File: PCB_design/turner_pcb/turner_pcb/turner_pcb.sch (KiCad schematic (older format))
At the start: 7 parts, among them P1 Digital, P2 Analog, P3 CONN_01X01, P4 CONN_01X01, P5 CONN_01X01, P6 CONN_01X01, U1 TMC2208_SILENTSTEPSTICK

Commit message: First version of working firmware.
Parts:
- added R1, R2: R, Resistor_SMD:R_0815_2038Metric_Pad1.20x4.05mm_HandSolder, symbol Device:R
- added R3: R, Resistor_SMD:R_01005_0402Metric_Pad0.57x0.30mm_HandSolder, symbol Device:R
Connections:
- wire segments 35 -> 50
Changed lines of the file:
@@
 	9350 1100 8700 1100
 Wire Wire Line
-	8700 1200 9350 1200
-Wire Wire Line
 	9350 1300 8700 1300
 Wire Wire Line
@@
 	8700 1900 9350 1900
 Wire Wire Line
-	9350 2000 8700 2000
-Wire Wire Line
 	8700 2100 9350 2100
 Wire Wire Line
@@
 Wire Wire Line
 	9350 2400 8700 2400
-Wire Wire Line
-	8700 2500 9350 2500
 $Comp
 L power:GND #PWR02
@@
 Wire Wire Line
 	10150 1100 10250 1100
-Wire Wire Line
-	10250 1100 10250 950
 $Comp
 L power:+5V #PWR03
@@
 	1    0    0    -1
 $EndComp
+$Comp
+L power:GND #PWR05
+U 1 1 5FFFE9D3
+P 7100 2550
+F 0 "#PWR05" H 7100 2300 50  0001 C CNN
+F 1 "GND" H 7105 2377 50  0000 C CNN
+F 2 "" H 7100 2550 50  0001 C CNN
+F 3 "" H 7100 2550 50  0001 C CNN
+	1    7100 2550
+	1    0    0    -1
+$EndComp
+Wire Wire Line
+	6950 2550 7100 2550
+$Comp
+L power:+5V #PWR07
+U 1 1 60000A42
+P 10250 750
+F 0 "#PWR07" H 10250 600 50  0001 C CNN
+F 1 "+5V" H 10265 923 50  0000 C CNN
+F 2 "" H 10250 750 50  0001 C CNN
+F 3 "" H 10250 750 50  0001 C CNN
+	1    10250 750
+	1    0    0    -1
+$EndComp
+Wire Wire Line
+	10250 750  10250 1100
+$Comp
+L power:+5V #PWR06
+U 1 1 600018A2
+P 5450 1450
+F 0 "#PWR06" H 5450 1300 50  0001 C CNN
+F 1 "+5V" H 5465 1623 50  0000 C CNN
+F 2 "" H 5450 1450 50  0001 C CNN
+F 3 "" H 5450 1450 50  0001 C CNN
+	1    5450 1450
+	1    0    0    -1
+$EndComp
+Wire Wire Line
+	5550 1450 5450 1450
+$Comp
+L Device:R R1
+U 1 1 600047F1
+P 7350 1150
+F 0 "R1" H 7420 1196 50  0000 L CNN
+F 1 "R" H 7420 1105 50  0000 L CNN
+F 2 "Resistor_SMD:R_0815_2038Metric_Pad1.20x4.05mm_HandSolder" V 7280 1150 50  0001 C CNN
+F 3 "~" H 7350 1150 50  0001 C CNN
+	1    7350 1150
+	1    0    0    -1
+$EndComp
+$Comp
+L Device:R R2
+U 1 1 60004CE6
+P 7600 1150
+F 0 "R2" H 7670 1196 50  0000 L CNN
+F 1 "R" H 7670 1105 50  0000 L CNN
+F 2 "Resistor_SMD:R_0815_2038Metric_Pad1.20x4.05mm_HandSolder" V 7530 1150 50  0001 C CNN
+F 3 "~" H 7600 1150 50  0001 C CNN
+	1    7600 1150
+	1    0    0    -1
+$EndComp
+Wire Wire Line
+	6950 1350 7350 1350
+Wire Wire Line
+	7350 1350 7350 1300
+Wire Wire Line
+	6950 1550 7600 1550
+Wire Wire Line
+	7600 1550 7600 1300
+Wire Wire Line
+	7600 1000 8250 1000
+Wire Wire Line
+	8250 1000 8250 1200
+Wire Wire Line
+	8250 1200 8700 1200
+Wire Wire Line
+	8700 1200 8700 1100
+Wire Wire Line
+	8700 1100 8400 1100
+Wire Wire Line
+	8400 1100 8400 900
+Wire Wire Line
+	8400 900  7350 900
+Wire Wire Line
+	7350 900  7350 1000
+Connection ~ 8700 1200
+Wire Wire Line
+	8700 1200 9350 1200
+Connection ~ 8700 1100
+$Comp
+L Device:R R3
+U 1 1 60009A47
+P 8200 2150
+F 0 "R3" H 8270 2196 50  0000 L CNN
+F 1 "R" H 8270 2105 50  0000 L CNN
+F 2 "Resistor_SMD:R_01005_0402Metric_Pad0.57x0.30mm_HandSolder" V 8130 2150 50  0001 C CNN
+F 3 "~" H 8200 2150 50  0001 C CNN
+	1    8200 2150
+	1    0    0    -1
+$EndComp
+Wire Wire Line
+	8200 2000 9350 2000
+Wire Wire Line
+	8200 2500 8200 2300
+Wire Wire Line
+	8200 2500 9350 2500
 $EndSCHEMATC

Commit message: first attempt at including tmc2208
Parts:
- removed P1: Digital, Socket_Arduino_Nano:Socket_Strip_Arduino_1x15, symbol Connector_Generic:Conn_01x15
- removed P2: Analog, Socket_Arduino_Nano:Socket_Strip_Arduino_1x15, symbol Connector_Generic:Conn_01x15
- removed P3, P4, P5, P6: CONN_01X01, Socket_Arduino_Nano:1pin_Nano, symbol Connector_Generic:Conn_01x01
- removed R1, R2: R, Resistor_SMD:R_0815_2038Metric_Pad1.20x4.05mm_HandSolder, symbol Device:R
- removed R3: R, Resistor_SMD:R_01005_0402Metric_Pad0.57x0.30mm_HandSolder, symbol Device:R
- added A1: Arduino_Nano_v3.x, Module:Arduino_Nano, symbol MCU_Module:Arduino_Nano_v3.x
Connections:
- net labels added: +12V, Direction, Enable, Step
- net labels removed: +3.3V, 0(Rx), 1(Tx), 10(**/SS), 11(**/MOSI), 12(MISO), 13(SCK), 2, 3(**), 4, 5(**), 6(**), 7, 8, 9(**), A0, A1, A2, A3, A4, A5, A6, A7, AREF, Reset, Vin
- wire segments 50 -> 21
- no-connect marks 4 -> 0
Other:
- note removed: "1"
- note removed: "Holes"
- note removed: "Shield for Arduino Nano"
- moved on the sheet: U1

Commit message: first complete version on pcb
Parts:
- added C1: C_Small, Capacitor_SMD:C_0603_1608Metric, symbol Device:C_Small
- added C2: C_Polarized, Capacitor_THT:CP_Radial_D8.0mm_P5.00mm, symbol Device:C_Polarized
- added General_IO1: Conn_02x03_Odd_Even, Connector_Molex:Molex_Micro-Fit_3.0_43045-0612_2x03_P3.00mm_Vertical, symbol Connector_Generic:Conn_02x03_Odd_Even
- added input_power1: Conn_01x02, Connector_Molex:Molex_Micro-Fit_3.0_43045-0212_2x01_P3.00mm_Vertical, symbol Connector_Generic:Conn_01x02
- added pot_input1, stepper1: Conn_02x02_Odd_Even, Connector_Molex:Molex_Micro-Fit_3.0_43045-0412_2x02_P3.00mm_Vertical, symbol Connector_Generic:Conn_02x02_Odd_Even
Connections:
- net +12V: now also A1.30 (VIN), C2.1, input_power1.2 (Pin_2)
- net +5V: now also C1.2, pot_input1.2 (Pin_2)
- net GND: now also C1.1, C2.2, General_IO1.1 (Pin_1), input_power1.1 (Pin_1), pot_input1.1 (Pin_1)
- net DA2: now reaches U1.JP2_3 (OA2)
- net DA2: now also stepper1.3 (Pin_3)
- net DA1: now reaches U1.JP2_4 (OA1)
- net DA1: now also stepper1.1 (Pin_1)
- net DB1: now reaches U1.JP2_5 (OB1)
- net DB1: now also stepper1.2 (Pin_2)
- net DB2: now reaches U1.JP2_6 (OB2)
- net DB2: now also stepper1.4 (Pin_4)
- net DIO3: now reaches A1.10 (D7)
- net DIO3: now also General_IO1.5 (Pin_5)
- net DIO4: now reaches A1.11 (D8)
- net DIO4: now also General_IO1.6 (Pin_6)
- net Pot: now reaches A1.19 (A0)
- net Pot: now also pot_input1.3 (Pin_3)
- net AO1: now reaches A1.20 (A1)
- net AO1: now also General_IO1.2 (Pin_2)
- net DIO1: now reaches A1.8 (D5)
- net DIO1: now also General_IO1.3 (Pin_3)
- net DIO2: now reaches A1.9 (D6)
- net DIO2: now also General_IO1.4 (Pin_4)

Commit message: worked on pcb design
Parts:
- removed U1: TMC2208_SILENTSTEPSTICK, TMC2208_SILENTSTEPSTICK:MODULE_TMC2208_SILENTSTEPSTICK, symbol TMC2208_SILENTSTEPSTICK:TMC2208_SILENTSTEPSTICK
- added A2: Pololu_Breakout_A4988, Module:Pololu_Breakout-16_15.2x20.3mm, symbol Driver_Motor:Pololu_Breakout_A4988
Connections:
- net +12V: now also A2.8 (VMOT)
- net +5V: now also General_IO1.2 (Pin_2), A2.2 (VDD)
- net Direction: now also A2.16 (DIR)
- net Enable: now also A2.9 (~ENABLE)
- net GND: now also A2.1 (GND), A2.13 (~RESET), A2.14 (~SLEEP), A2.7 (GND)
- net Step: now also A2.15 (STEP)
- net MS1: now reaches A1.12 (D9)
- net MS1: now also A2.10 (MS1)
- net MS2: now reaches A1.13 (D10)
- net MS2: now also A2.11 (MS2)
- net MS3: now reaches A1.14 (D11)
- net MS3: now also A2.12 (MS3)
- net AO1: no longer names the net of A1.20 (A1)
- net AO1: no longer General_IO1.2 (Pin_2)
- net DA1 renamed M1A
- net M1A: now also A2.4 (1A)
- net DA2 renamed M2A
- net M2A: now also A2.5 (2A)
- net DB1 renamed M1B
- net M1B: now also A2.3 (1B)
- net DB2 renamed M2B
- net M2B: now also A2.6 (2B)
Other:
- moved on the sheet: C1, C2

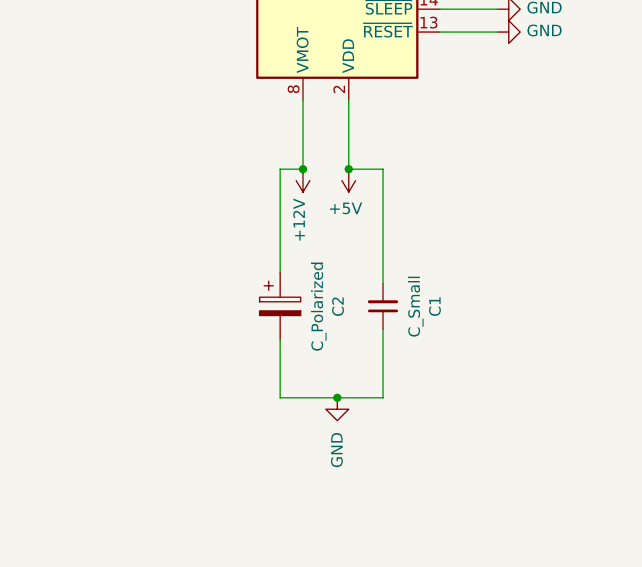
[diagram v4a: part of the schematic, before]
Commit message: pcb design V1.0 sent to JLCPCB
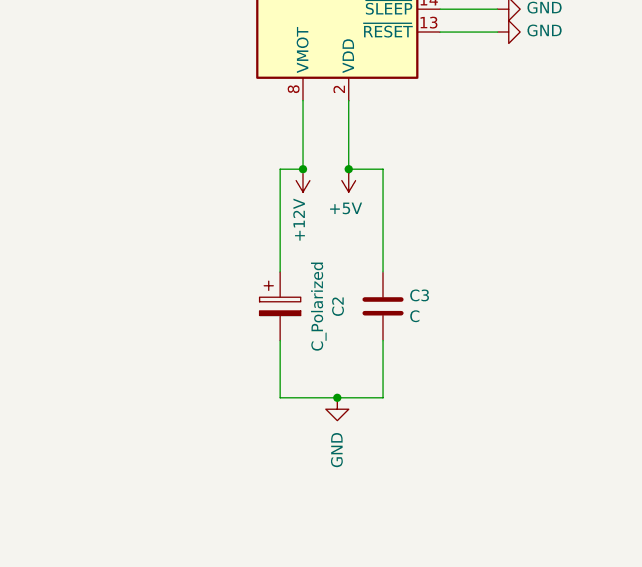
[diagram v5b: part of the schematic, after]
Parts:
- removed C1: C_Small, Capacitor_SMD:C_0603_1608Metric, symbol Device:C_Small
- added C3: C, Capacitor_SMD:C_0603_1608Metric_Pad1.08x0.95mm_HandSolder, symbol Device:C
- C2: footprint Capacitor_THT:CP_Radial_D8.0mm_P5.00mm -> Capacitor_THT:CP_Radial_D8.0mm_P3.80mm
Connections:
- net +5V: now also C3.1
- net GND: now also C3.2
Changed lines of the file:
@@
-$EndComp
-$Comp
-L Device:C_Small C1
-U 1 1 606D78AE
-P 8750 3450
-F 0 "C1" V 8521 3450 50  0000 C CNN
-F 1 "C_Small" V 8612 3450 50  0000 C CNN
-F 2 "Capacitor_SMD:C_0603_1608Metric" H 8750 3450 50  0001 C CNN
-F 3 "~" H 8750 3450 50  0001 C CNN
-	1    8750 3450
-	-1   0    0    1
 $EndComp
 $Comp
@@
 F 0 "C2" V 8555 3450 50  0000 C CNN
 F 1 "C_Polarized" V 8464 3450 50  0000 C CNN
-F 2 "Capacitor_THT:CP_Radial_D8.0mm_P5.00mm" H 8338 3300 50  0001 C CNN
+F 2 "Capacitor_THT:CP_Radial_D8.0mm_P3.80mm" H 8338 3300 50  0001 C CNN
 F 3 "~" H 8300 3450 50  0001 C CNN
 	1    8300 3450
@@
 $EndComp
 Wire Wire Line
-	8750 3350 8750 2850
-Wire Wire Line
 	8300 3300 8300 2850
 Wire Wire Line
@@
 Wire Wire Line
 	8300 3600 8300 3850
-Wire Wire Line
-	8750 3550 8750 3850
-Wire Wire Line
-	8750 3850 8550 3850
-Connection ~ 8550 3850
 $Comp
 L Connector_Generic:Conn_01x02 input_power1
@@
 Wire Wire Line
 	4600 2550 4400 2550
+$Comp
+L Device:C C3
+U 1 1 606FAE10
+P 8750 3450
+F 0 "C3" H 8865 3496 50  0000 L CNN
+F 1 "C" H 8865 3405 50  0000 L CNN
+F 2 "Capacitor_SMD:C_0603_1608Metric_Pad1.08x0.95mm_HandSolder" H 8788 3300 50  0001 C CNN
+F 3 "~" H 8750 3450 50  0001 C CNN
+	1    8750 3450
+	1    0    0    -1
+$EndComp
+Wire Wire Line
+	8750 2850 8750 3300
+Wire Wire Line
+	8750 3600 8750 3850
+Wire Wire Line
+	8750 3850 8550 3850
+Connection ~ 8550 3850
 $EndSCHEMATC
